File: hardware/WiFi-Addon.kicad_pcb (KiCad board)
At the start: 2 copper layers, 44 x 28 mm, 26 parts, among them J3 USB_B_Micro, U1 AMS1117-3.3, U2 ESP-12F, U3 CH340G

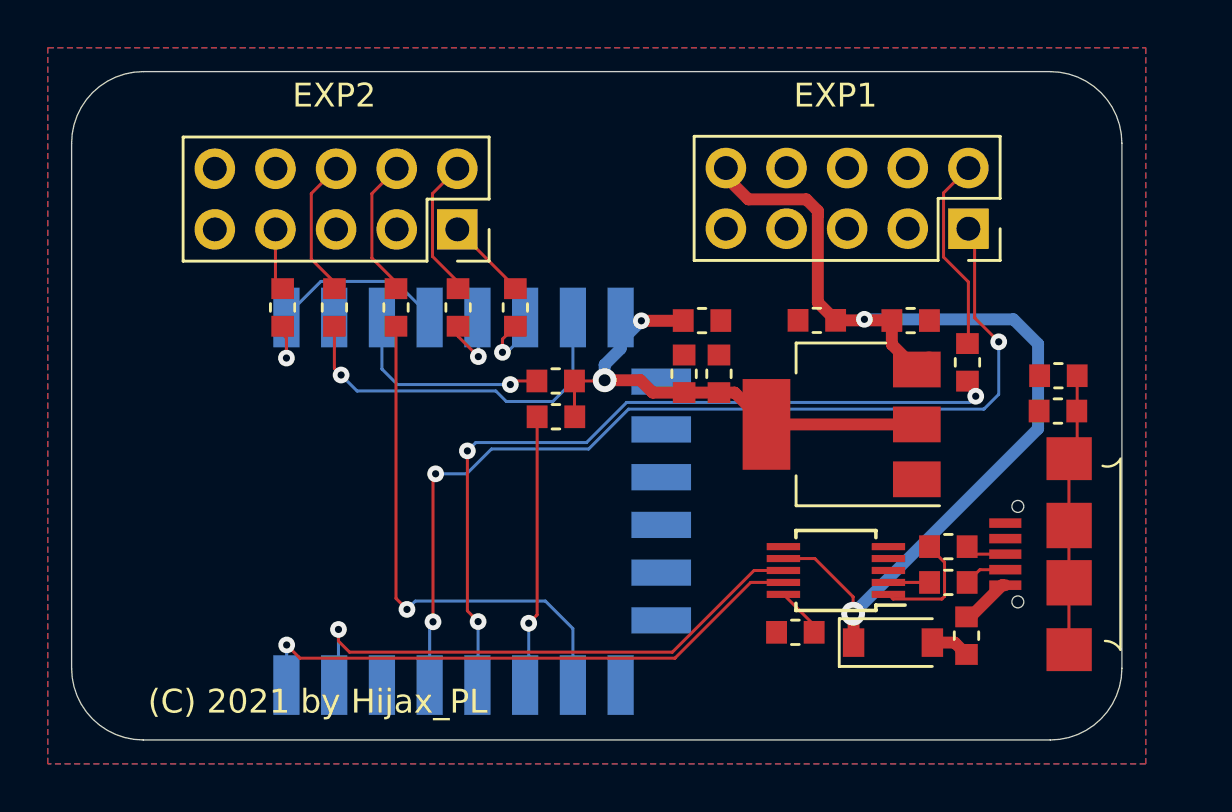
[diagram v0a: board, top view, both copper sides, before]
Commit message: Correcting footprint, and adding manufacturing markers
Gerber files & interactive BOM generated
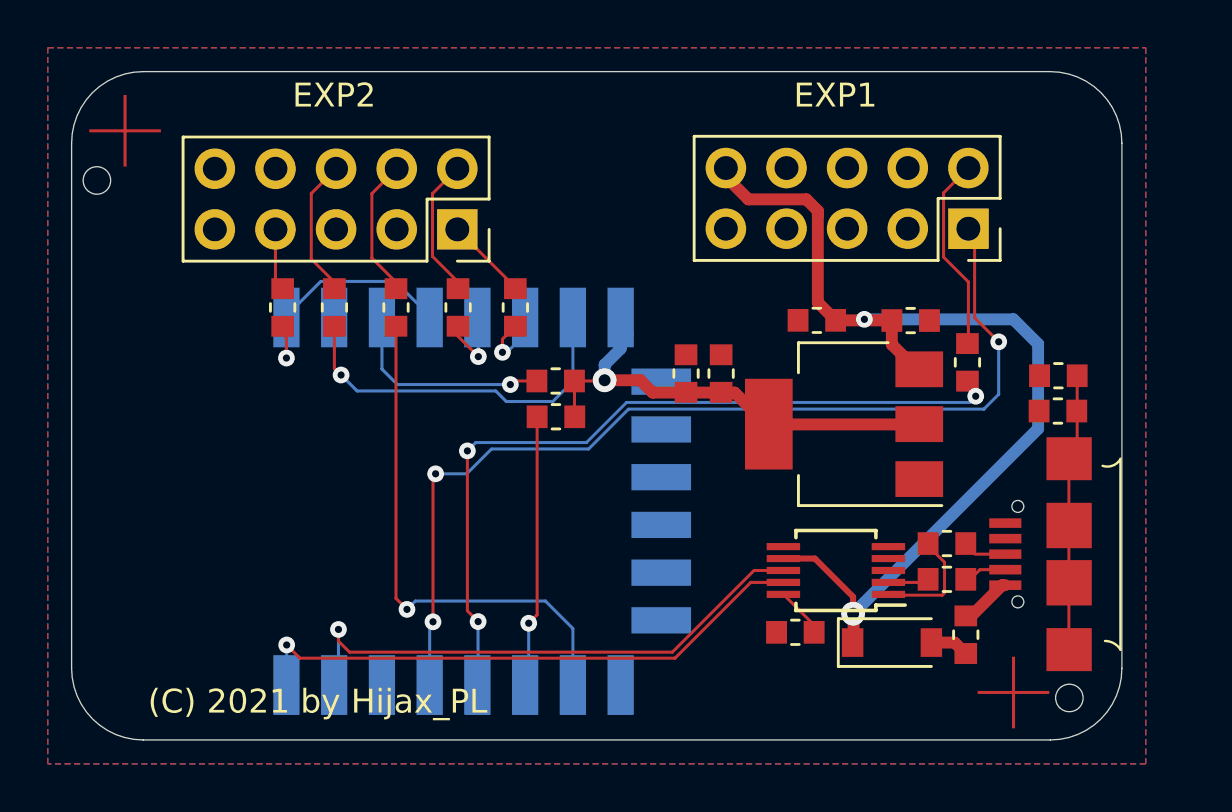
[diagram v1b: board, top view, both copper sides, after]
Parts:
- removed C5: 10uF, PrntrBoardV2:C_0603_1608Metric
- added FID1: Fiducial, PrntrBoardV2:Fiducial_1mm_Dia_2.54mm_Outer_CopperTop, F.Cu at (30.2, 97.5)
- added FID2: Fiducial, PrntrBoardV2:Fiducial_1mm_Dia_2.54mm_Outer_CopperTop, F.Cu at (67.5, 121.0)
- added H1: JLC Tooling Hole, PrntrBoardV2:JLC_Tool_hole, F.Cu at (88.5, 110.8)
- added H2: JLC Tooling Hole, PrntrBoardV2:JLC_Tool_hole, F.Cu at (88.5, 113.0)
- added LOGO1: Logo_Open_Hardware_Small, Symbol:OSHW-Logo2_9.8x8mm_SilkScreen, B.Cu at (67.0, 116.8)
- moved R10 0.14 mm to (64.7, 116.3)
- moved R11 0.14 mm to (64.7, 114.8)
- moved U1 0.10 mm to (60.4, 109.8)
- moved C4 0.09 mm to (55.2, 107.7)
- moved C3 0.08 mm to (53.7, 107.7)
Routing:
- net 3.3V: track 21.7 -> 19.1 mm, vias 2 -> 1
- net 5V: track 42.6 -> 41.9 mm
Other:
- board text added: "EXP1"
- board text added: "EXP2"
- board text added: "JLCJLCJLCJLC"
- board text added: "WIFI Module V1"
- board text removed: "PrntrBoardV2 WIFI Module"

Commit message: Correction of header placement
Proper layer and spacing.
Plus small jumper to select USB or VIN power for WIFi
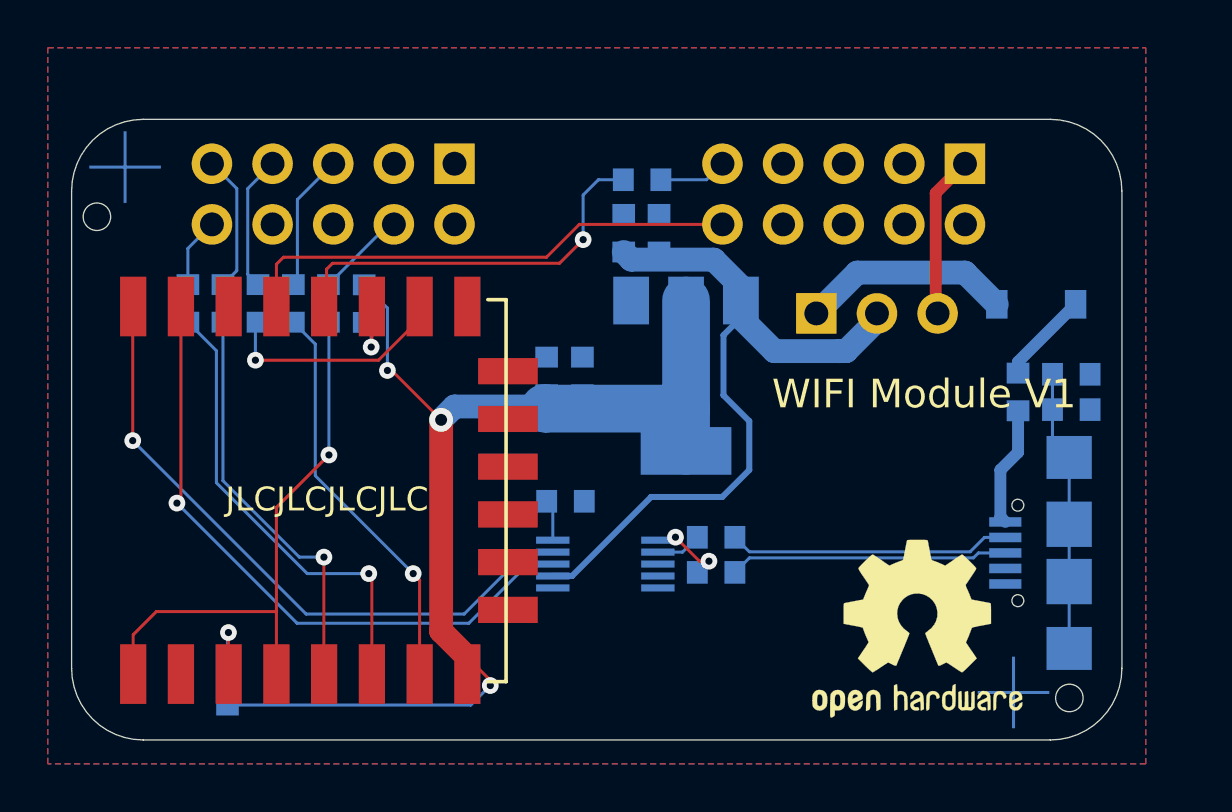
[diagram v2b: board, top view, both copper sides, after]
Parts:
- added J1: PWR, Connector_PinHeader_2.54mm:PinHeader_1x03_P2.54mm_Horizontal, B.Cu at (59.2, 105.1)
- C1, C19, C2, C3, C4, C6, D1, EXP1, EXP2, F1, FID1, FID2, J3, R1, R10, R11, R12, R2, R3, R4, R5, R6, R7, R8, U1, U3: moved to B.Cu
- LOGO1, U2: moved to F.Cu
- moved R7 18.8 mm to (34.5, 120.8), turned to -90 degrees
- moved R3 15.6 mm to (51.9, 99.5), turned to 180 degrees
- moved D1 15.4 mm to (68.4, 104.8)
- moved U2 15.0 mm to (30.6, 119.5), turned to 90 degrees
- moved R1 13.7 mm to (32.9, 104.7)
- moved C2 11.2 mm to (52.6, 101.8), turned to 90 degrees
- moved C6 11.1 mm to (48.7, 113.0), turned to 180 degrees
- moved F1 10.4 mm to (67.7, 108.4), turned to 90 degrees
- moved R4 9.85 mm to (34.3, 104.7)
- moved R10 9.83 mm to (55.0, 114.5)
- moved R11 9.75 mm to (55.0, 116.0)
- moved U3 9.66 mm to (50.4, 115.6)
- moved R8 9.32 mm to (40.3, 104.7), turned to -90 degrees
- moved C1 8.88 mm to (51.1, 101.8), turned to 90 degrees
- moved U1 6.92 mm to (53.7, 107.7), turned to -90 degrees
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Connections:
- D1 pad 1: 5V -> /VBUS
- EXP1 pad 1: /GPIO4 -> /VIN
- EXP1 pad 10: 5V -> /GPIO4
- EXP1 pad 2: Net-(EXP1-Pad2) -> GND
- EXP1 pad 9: GND -> Net-(EXP1-Pad9)
- EXP2 pad 1: /E_MISO -> (no net)
- EXP2 pad 10: (no net) -> /E_MISO
- EXP2 pad 2: /E_SCK -> GND
- EXP2 pad 4: /CSEL -> /E_RST
- EXP2 pad 5: (no net) -> /E_MOSI
- EXP2 pad 6: /E_MOSI -> (no net)
- EXP2 pad 7: /E_RST -> /CSEL
- EXP2 pad 9: GND -> /E_SCK
- R3 pad 1: Net-(EXP1-Pad2) -> Net-(EXP1-Pad9)
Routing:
- net 3.3V: track 19.1 -> 47.3 mm, vias 1 -> 3
- net /GPIO4: track 40.3 -> 21.8 mm, vias 3 -> 0
- net /MISO: track 2.58 -> 18.7 mm
- net /BOOT: track 31.9 -> 16.4 mm, vias 3 -> 1
- net /SCK: track 2.80 -> 16.4 mm
- net /~CS: track 21.6 -> 8.94 mm
- net /RST: track 9.73 -> 22.3 mm
- net /D+: track 1.28 -> 11.7 mm
- net /D-: track 1.82 -> 11.8 mm
- net 5V: track 41.9 -> 33.1 mm, vias 2 -> 0
- net /VBUS: track 0.00 -> 8.82 mm
- net Net-(R8-Pad2): track 10.5 -> 1.75 mm
- net Net-(EXP1-Pad2): track 7.88 -> 0.00 mm
- net /VIN: track 0.00 -> 6.70 mm
- net /EN: track 8.28 -> 2.51 mm
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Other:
- board size 44 x 28 mm -> 44 x 26 mm
- board text added: "VIN - USB POWER"
- board text removed: "EXP1"
- board text removed: "EXP2"

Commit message: Added some more information to schema
Added datasheet links to ESP-12F and ESP8266EX
Some additional info on schematics and repositioning of resistors for better understed of their purpose.
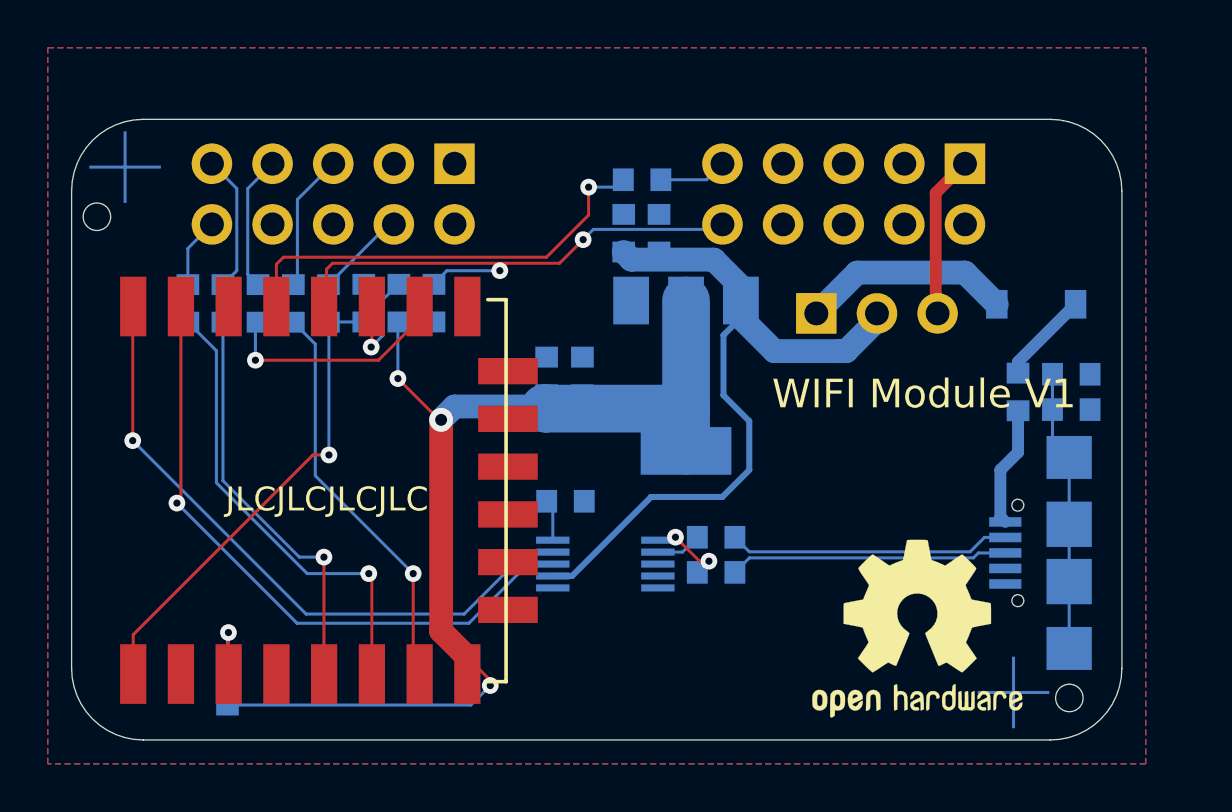
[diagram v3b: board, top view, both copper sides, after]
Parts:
- added C5: 0.1uF, PrntrBoardV2:C_0603_1608Metric, B.Cu at (40.2, 104.7)
- added R13: 10k, PrntrBoardV2:R_0603_1608Metric, B.Cu at (43.2, 104.7)
- moved R8 1.45 mm to (41.7, 104.7), turned to 90 degrees
- turned R1 to -90 degrees
- turned R2 to -90 degrees
- turned R4 to -90 degrees
- turned R5 to -90 degrees
- turned R6 to -90 degrees
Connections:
- EXP1 pad 10: /GPIO4 -> /DATA_RDY
- R1 pad 1: /MISO -> /E_MISO
- R1 pad 2: /E_MISO -> /MISO
- R2 pad 1: /RST -> /E_RST
- R2 pad 2: /E_RST -> /RST
- R3 pad 2: /BOOT -> /TRF_RDY
- R4 pad 1: /SCK -> /E_SCK
- R4 pad 2: /E_SCK -> /SCK
- R5 pad 1: /~CS -> /CSEL
- R5 pad 2: /CSEL -> Net-(R5-Pad2)
- R6 pad 1: /MOSI -> /E_MOSI
- R6 pad 2: /E_MOSI -> /MOSI
- U2 pad 10: /~CS -> Net-(R5-Pad2)
- U2 pad 12: /BOOT -> /DATA_RDY
- U2 pad 13: /GPIO4 -> /TRF_RDY
- U2 pad 4: /RST -> (no net)
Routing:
- net /DATA_RDY: track 0.00 -> 22.1 mm, vias 0 -> 2
- net /GPIO4: track 21.8 -> 0.00 mm
- net /TRF_RDY: track 0.00 -> 19.2 mm, vias 0 -> 1
- net /BOOT: track 16.4 -> 0.00 mm, vias 1 -> 0
- net Net-(R5-Pad2): track 0.00 -> 8.94 mm, vias 0 -> 1
- net /~CS: track 8.94 -> 0.00 mm, vias 1 -> 0
- net /RST: track 22.3 -> 19.3 mm
- net Net-(R8-Pad2): track 1.75 -> 4.11 mm
- net 3.3V: track 47.3 -> 46.6 mm
